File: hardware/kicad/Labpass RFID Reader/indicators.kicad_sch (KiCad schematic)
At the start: 4 parts, among them J2 Conn_01x04

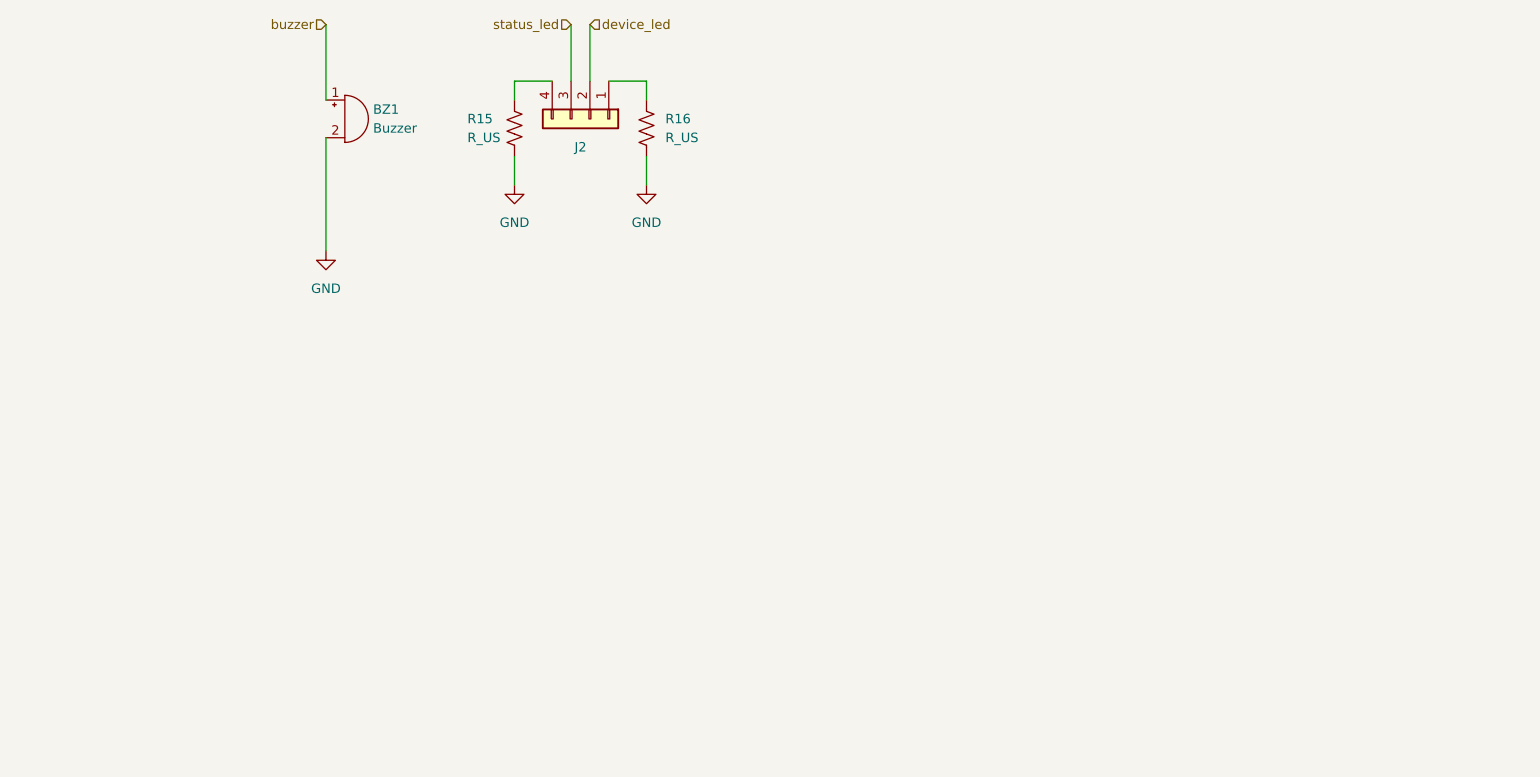
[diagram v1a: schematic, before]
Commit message: Add RGB LEDs with 4 wires
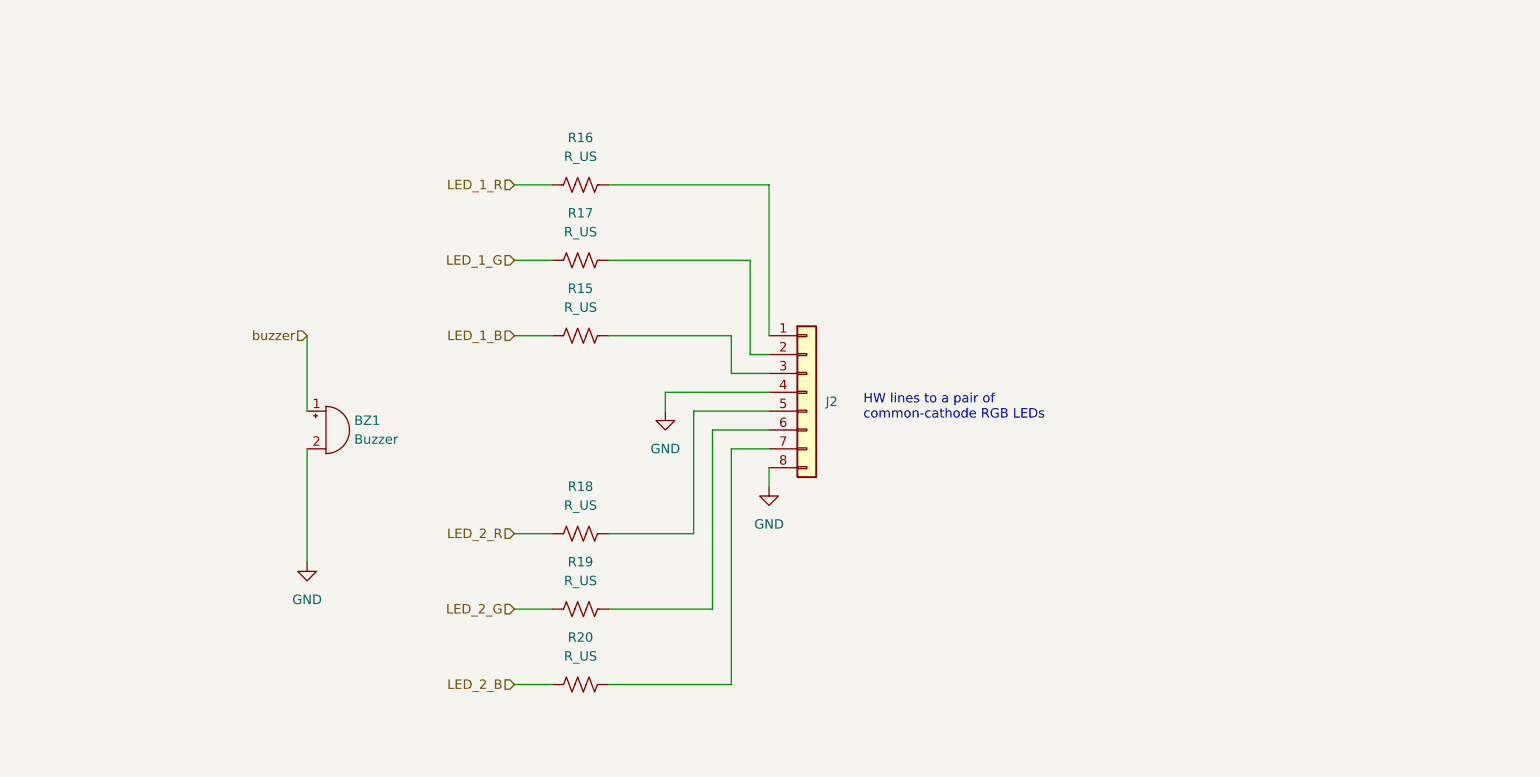
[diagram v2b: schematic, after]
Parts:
- added R17, R18, R19, R20: R_US, Resistor_SMD:R_0603_1608Metric, symbol Device:R_US
- J2: value Conn_01x04 -> (none); footprint Connector_PinHeader_1.27mm:PinHeader_1x04_P1.27mm_Vertical_SMD_Pin1Left -> (none); symbol Connector_Generic:Conn_01x04 -> Connector_Generic:Conn_01x08
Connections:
- net GND: now also J2.4 (Pin_4), J2.8 (Pin_8); no longer R15.2, R16.2
- net LED_1_B: now reaches R15.1
- net LED_1_B: no longer J2.4 (Pin_4)
- net at J2.1 (Pin_1): now also R16.2; no longer R16.1
- net device_led: no longer names the net of J2.2 (Pin_2)
- net device_led: now also R17.2
- net status_led: no longer names the net of J2.3 (Pin_3)
- net status_led: now also R15.2
- new net: J2.6 (Pin_6), R19.2
- new net: J2.5 (Pin_5), R18.2
- new net: J2.7 (Pin_7), R20.2
- new net LED_1_G: R17.1
- new net LED_1_R: R16.1
- new net LED_2_B: R20.1
- new net LED_2_G: R19.1
- new net LED_2_R: R18.1
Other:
- note added: "HW lines to a pair of common-cathode RGB LEDs"
- moved on the sheet: BZ1

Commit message: last-minute fixes
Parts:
- J2: value (none) -> Conn_01x04; footprint (none) -> Connector_PinHeader_1.27mm:PinHeader_1x08_P1.27mm_Vertical_SMD_Pin1Left
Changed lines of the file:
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@@
       (effects (font (size 1.27 1.27)) (justify left))
     )
-    (property "Value" "" (id 1) (at 144.78 91.44 90)
+    (property "Value" "Conn_01x04" (id 1) (at 144.78 91.44 90)
       (effects (font (size 1.27 1.27)) hide)
     )
-    (property "Footprint" "" (id 2) (at 138.43 90.17 0)
+    (property "Footprint" "Connector_PinHeader_1.27mm:PinHeader_1x08_P1.27mm_Vertical_SMD_Pin1Left" (id 2) (at 138.43 90.17 0)
       (effects (font (size 1.27 1.27)) hide)
     )

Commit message: kicad backups
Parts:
- J2: value Conn_01x04 -> Conn_01x08; footprint Connector_PinHeader_1.27mm:PinHeader_1x08_P1.27mm_Vertical_SMD_Pin1Left -> Connector_PinHeader_2.54mm:PinHeader_1x08_P2.54mm_Vertical_SMD_Pin1Right
- R15, R16, R17, R18, R19, R20: value R_US -> 1k
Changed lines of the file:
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@@
     (in_bom yes) (on_board yes) (fields_autoplaced)
     (property "Reference" "R16" (id 0) (at 107.95 55.88 90))
-    (property "Value" "R_US" (id 1) (at 107.95 58.42 90))
+    (property "Value" "1k" (id 1) (at 107.95 58.42 90))
     (property "Footprint" "Resistor_SMD:R_0603_1608Metric" (id 2) (at 108.204 61.214 90)
       (effects (font (size 1.27 1.27)) hide)
@@
     (in_bom yes) (on_board yes) (fields_autoplaced)
     (property "Reference" "R19" (id 0) (at 107.95 113.03 90))
-    (property "Value" "R_US" (id 1) (at 107.95 115.57 90))
+    (property "Value" "1k" (id 1) (at 107.95 115.57 90))
     (property "Footprint" "Resistor_SMD:R_0603_1608Metric" (id 2) (at 108.204 118.364 90)
       (effects (font (size 1.27 1.27)) hide)
@@
     (in_bom yes) (on_board yes) (fields_autoplaced)
     (property "Reference" "R18" (id 0) (at 107.95 102.87 90))
-    (property "Value" "R_US" (id 1) (at 107.95 105.41 90))
+    (property "Value" "1k" (id 1) (at 107.95 105.41 90))
     (property "Footprint" "Resistor_SMD:R_0603_1608Metric" (id 2) (at 108.204 108.204 90)
       (effects (font (size 1.27 1.27)) hide)
@@
     (in_bom yes) (on_board yes) (fields_autoplaced)
     (property "Reference" "R15" (id 0) (at 107.95 76.2 90))
-    (property "Value" "R_US" (id 1) (at 107.95 78.74 90))
+    (property "Value" "1k" (id 1) (at 107.95 78.74 90))
     (property "Footprint" "Resistor_SMD:R_0603_1608Metric" (id 2) (at 108.204 81.534 90)
       (effects (font (size 1.27 1.27)) hide)
@@
     (in_bom yes) (on_board yes) (fields_autoplaced)
     (property "Reference" "R17" (id 0) (at 107.95 66.04 90))
-    (property "Value" "R_US" (id 1) (at 107.95 68.58 90))
+    (property "Value" "1k" (id 1) (at 107.95 68.58 90))
     (property "Footprint" "Resistor_SMD:R_0603_1608Metric" (id 2) (at 108.204 71.374 90)
       (effects (font (size 1.27 1.27)) hide)
@@
       (effects (font (size 1.27 1.27)) (justify left))
     )
-    (property "Value" "Conn_01x04" (id 1) (at 144.78 91.44 90)
+    (property "Value" "Conn_01x08" (id 1) (at 144.78 91.44 90)
       (effects (font (size 1.27 1.27)) hide)
     )
-    (property "Footprint" "Connector_PinHeader_1.27mm:PinHeader_1x08_P1.27mm_Vertical_SMD_Pin1Left" (id 2) (at 138.43 90.17 0)
+    (property "Footprint" "Connector_PinHeader_2.54mm:PinHeader_1x08_P2.54mm_Vertical_SMD_Pin1Right" (id 2) (at 138.43 90.17 0)
       (effects (font (size 1.27 1.27)) hide)
     )
@@
     (in_bom yes) (on_board yes) (fields_autoplaced)
     (property "Reference" "R20" (id 0) (at 107.95 123.19 90))
-    (property "Value" "R_US" (id 1) (at 107.95 125.73 90))
+    (property "Value" "1k" (id 1) (at 107.95 125.73 90))
     (property "Footprint" "Resistor_SMD:R_0603_1608Metric" (id 2) (at 108.204 128.524 90)
       (effects (font (size 1.27 1.27)) hide)

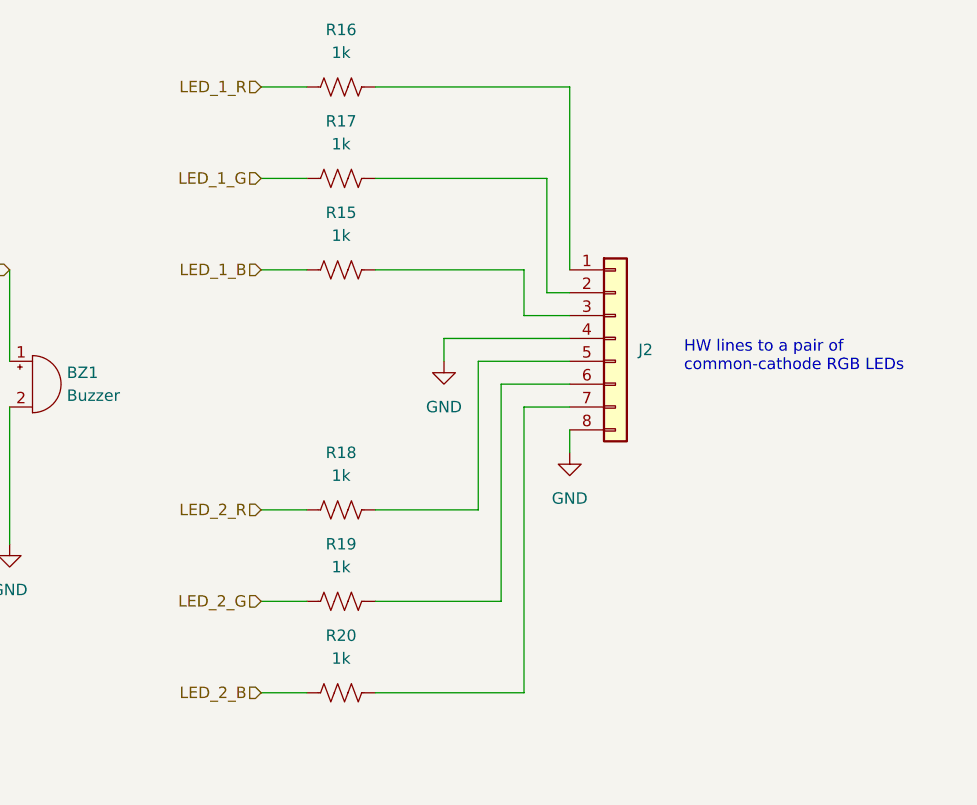
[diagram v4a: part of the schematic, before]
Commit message: Several fixes
* EA and I2C were backwards
* Adding missing Crx into HF receive path
* Better header size and placement
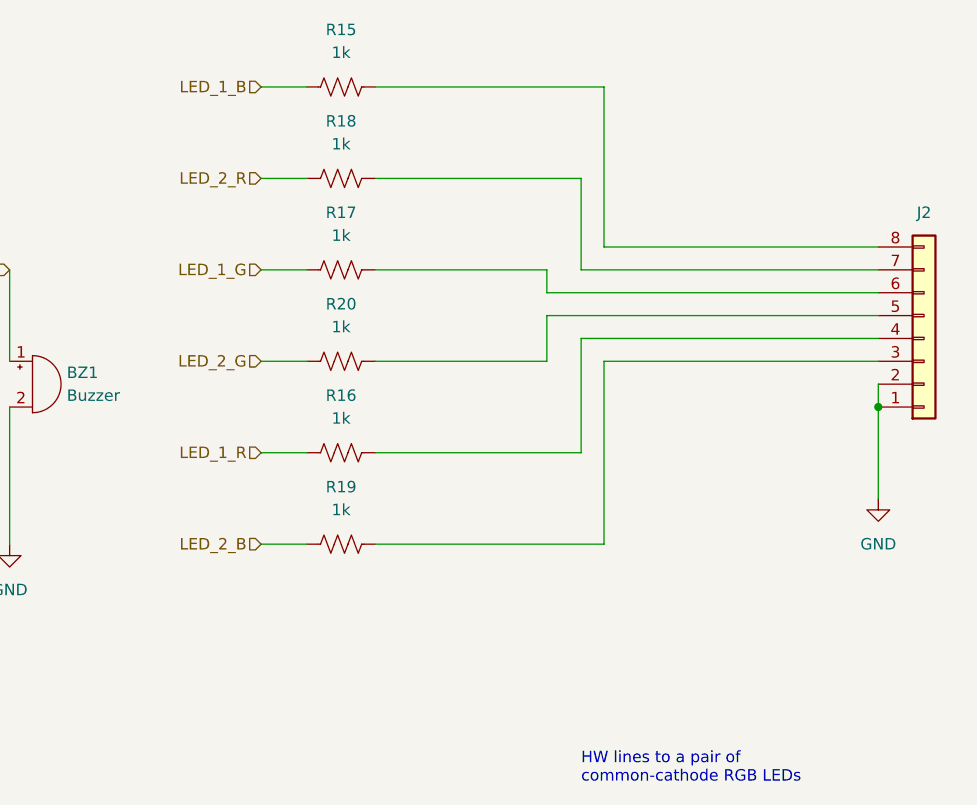
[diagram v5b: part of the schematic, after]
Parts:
- J2: value Conn_01x08 -> (none); footprint Connector_PinHeader_2.54mm:PinHeader_1x08_P2.54mm_Vertical_SMD_Pin1Right -> (none)
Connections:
- net GND: now also J2.1 (Pin_1), J2.2 (Pin_2); no longer J2.4 (Pin_4), J2.8 (Pin_8)
- net LED_2_B: now also R19.1; no longer R20.1
- net LED_2_G: now also R20.1; no longer R19.1
- net at R16.2: now also J2.4 (Pin_4); no longer J2.1 (Pin_1)
- net at R19.2: now also J2.3 (Pin_3); no longer J2.6 (Pin_6)
- net at R18.2: now also J2.7 (Pin_7); no longer J2.5 (Pin_5)
- net at R15.2: now also J2.8 (Pin_8); no longer J2.3 (Pin_3)
- net at R17.2: now also J2.6 (Pin_6); no longer J2.2 (Pin_2)
- net at R20.2: now also J2.5 (Pin_5); no longer J2.7 (Pin_7)
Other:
- moved on the sheet: J2, R15, R16, R17, R18, R19, R20
